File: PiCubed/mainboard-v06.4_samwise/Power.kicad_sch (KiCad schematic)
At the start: 53 parts, among them J14 Conn_01x08_Horizontal, J19 35362-0650, U17 BQ25883RGER, U21 TPS7A4501DCQT, U4 ADM1176-1ARMZ-R7, U5 TPS54226PWPR, U6 LT3652HVIMSE#PBF

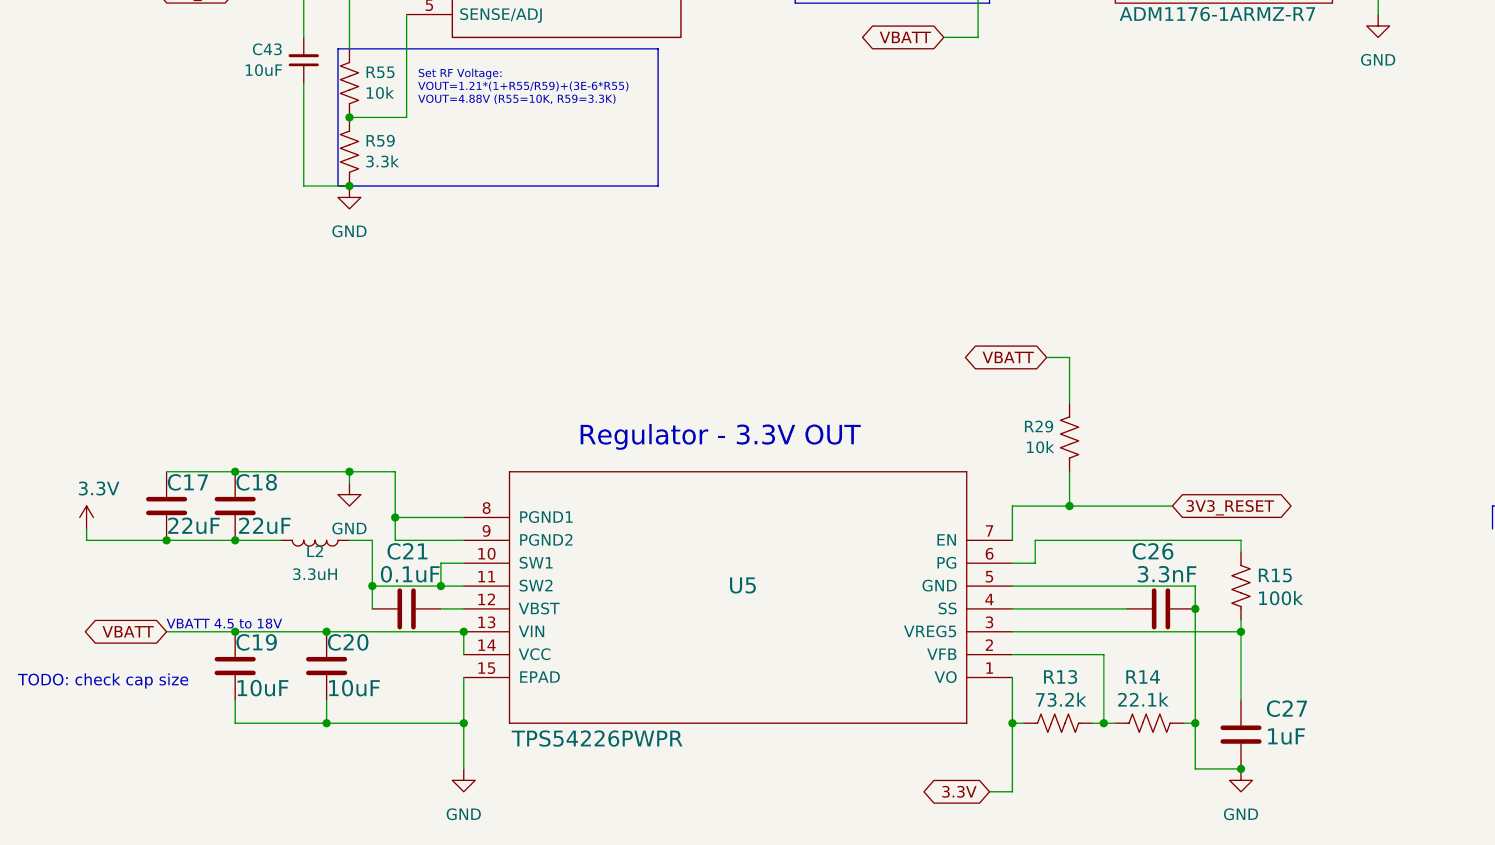
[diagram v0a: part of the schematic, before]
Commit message: 3v3 shunt diode added
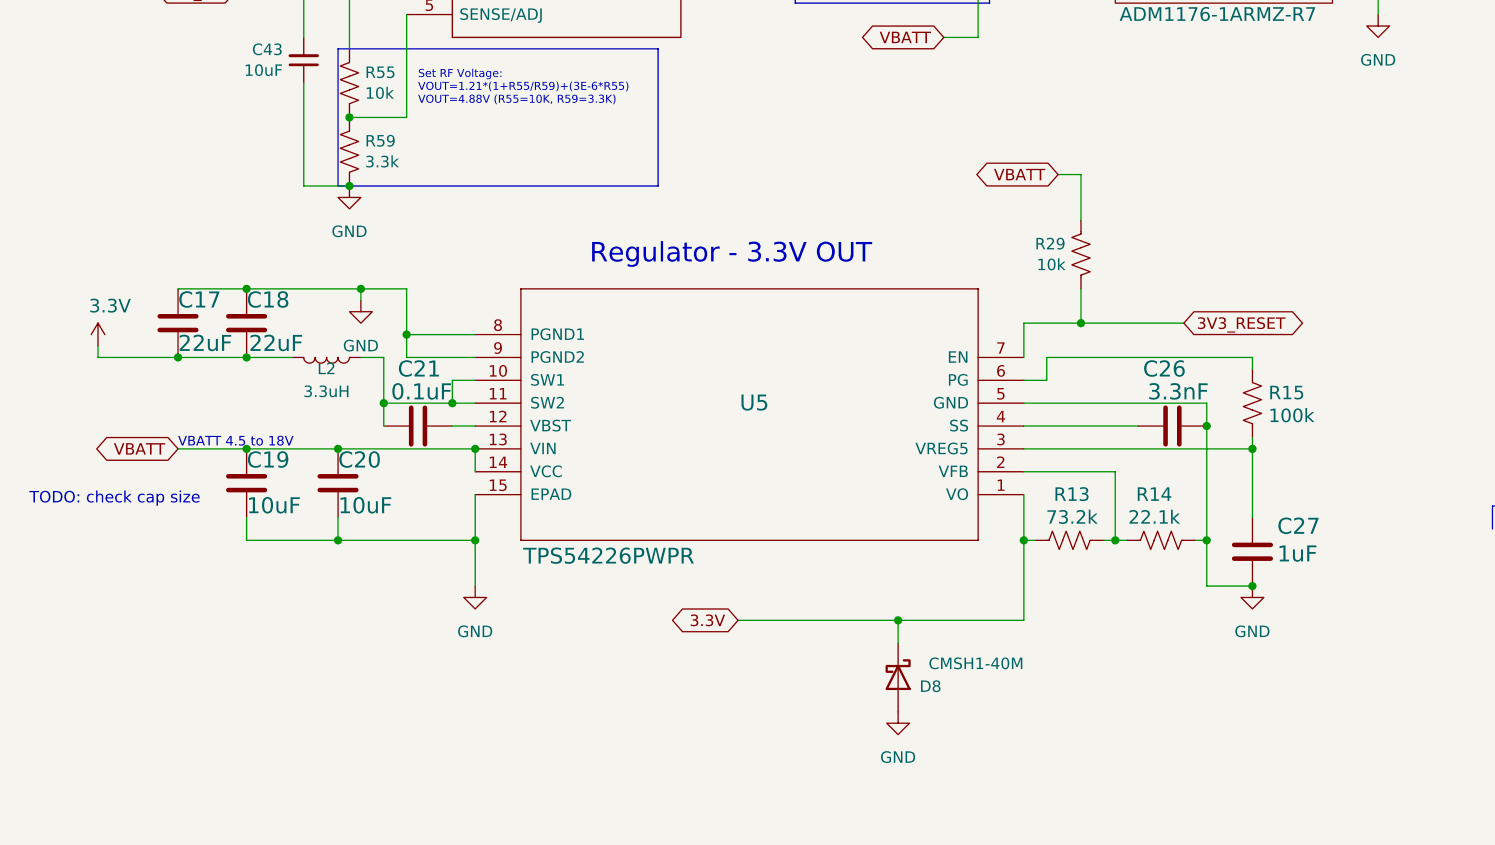
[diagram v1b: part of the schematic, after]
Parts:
- added D8: CMSH1-40M, ssi_diode:DIOM5226X262N, symbol Device:D_Schottky
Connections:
- net 3.3V: now also D8.1 (K)
- net GND: now also D8.2 (A)
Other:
- moved on the sheet: C17, C18, C19, C20, C21, C26, C27, L2, R13, R14, R15, R29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
